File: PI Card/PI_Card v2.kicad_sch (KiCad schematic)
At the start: 20 parts, among them J1 Conn_02x20_Odd_Even, J2 Conn_02x20_Odd_Even, J3 Conn_01x03_Pin, J4 Conn_01x02, J5 Conn_02x40_Odd_Even, J6 Conn_01x03_Pin, SW1 SW_Push

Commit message: Repositioned Connections
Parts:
- D4: value PTVS5V0Z1USK -> SMAJ5.0A; footprint Diode_SMD:Nexperia_DSN1608-2_1.6x0.8mm -> Diode_SMD:D_SMA_Handsoldering
- H1, H2, H3, H4: footprint MountingHole:MountingHole_3.2mm_M3 -> MountingHole:MountingHole_2.2mm_M2
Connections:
- net GPIO10: now also J5.13 (Pin_13); no longer J5.19 (Pin_19)
- net GPIO11: now also J5.17 (Pin_17); no longer J5.23 (Pin_23)
- net GPIO12: now also J5.20 (Pin_20); no longer J5.32 (Pin_32)
- net GPIO13: now also J5.25 (Pin_25); no longer J5.33 (Pin_33)
- net GPIO14: now also J5.2 (Pin_2); no longer J5.8 (Pin_8)
- net GPIO15: now also J5.4 (Pin_4); no longer J5.10 (Pin_10)
- net GPIO16: now also J5.22 (Pin_22); no longer J5.36 (Pin_36)
- net GPIO17: now also J5.7 (Pin_7); no longer J5.11 (Pin_11)
- net GPIO18: now also J5.6 (Pin_6); no longer J5.12 (Pin_12)
- net GPIO19: now also J5.27 (Pin_27); no longer J5.35 (Pin_35)
- net GPIO2: now also J5.1 (Pin_1); no longer J5.3 (Pin_3)
- net GPIO20: now also J5.24 (Pin_24); no longer J5.38 (Pin_38)
- net GPIO21: now also J5.26 (Pin_26); no longer J5.40 (Pin_40)
- net GPIO22: now also J5.11 (Pin_11); no longer J5.15 (Pin_15)
- net GPIO23: now also J5.8 (Pin_8); no longer J5.16 (Pin_16)
- net GPIO24: now also J5.10 (Pin_10); no longer J5.18 (Pin_18)
- net GPIO25: now also J5.12 (Pin_12); no longer J5.22 (Pin_22)
- net GPIO26: now also J5.29 (Pin_29); no longer J5.37 (Pin_37)
- net GPIO27: now also J5.9 (Pin_9); no longer J5.13 (Pin_13)
- net GPIO3: now also J5.3 (Pin_3); no longer J5.5 (Pin_5)
- net GPIO4: now also J5.5 (Pin_5); no longer J5.7 (Pin_7)
- net GPIO5: now also J5.21 (Pin_21); no longer J5.29 (Pin_29)
- net GPIO6: now also J5.23 (Pin_23); no longer J5.31 (Pin_31)
- net GPIO7: now also J5.16 (Pin_16); no longer J5.26 (Pin_26)
- net GPIO8: now also J5.14 (Pin_14); no longer J5.24 (Pin_24)
- net GPIO9: now also J5.15 (Pin_15); no longer J5.21 (Pin_21)
- net ID_SC: now also J5.18 (Pin_18); no longer J5.28 (Pin_28)
- net ID_SD: now also J5.19 (Pin_19); no longer J5.27 (Pin_27)

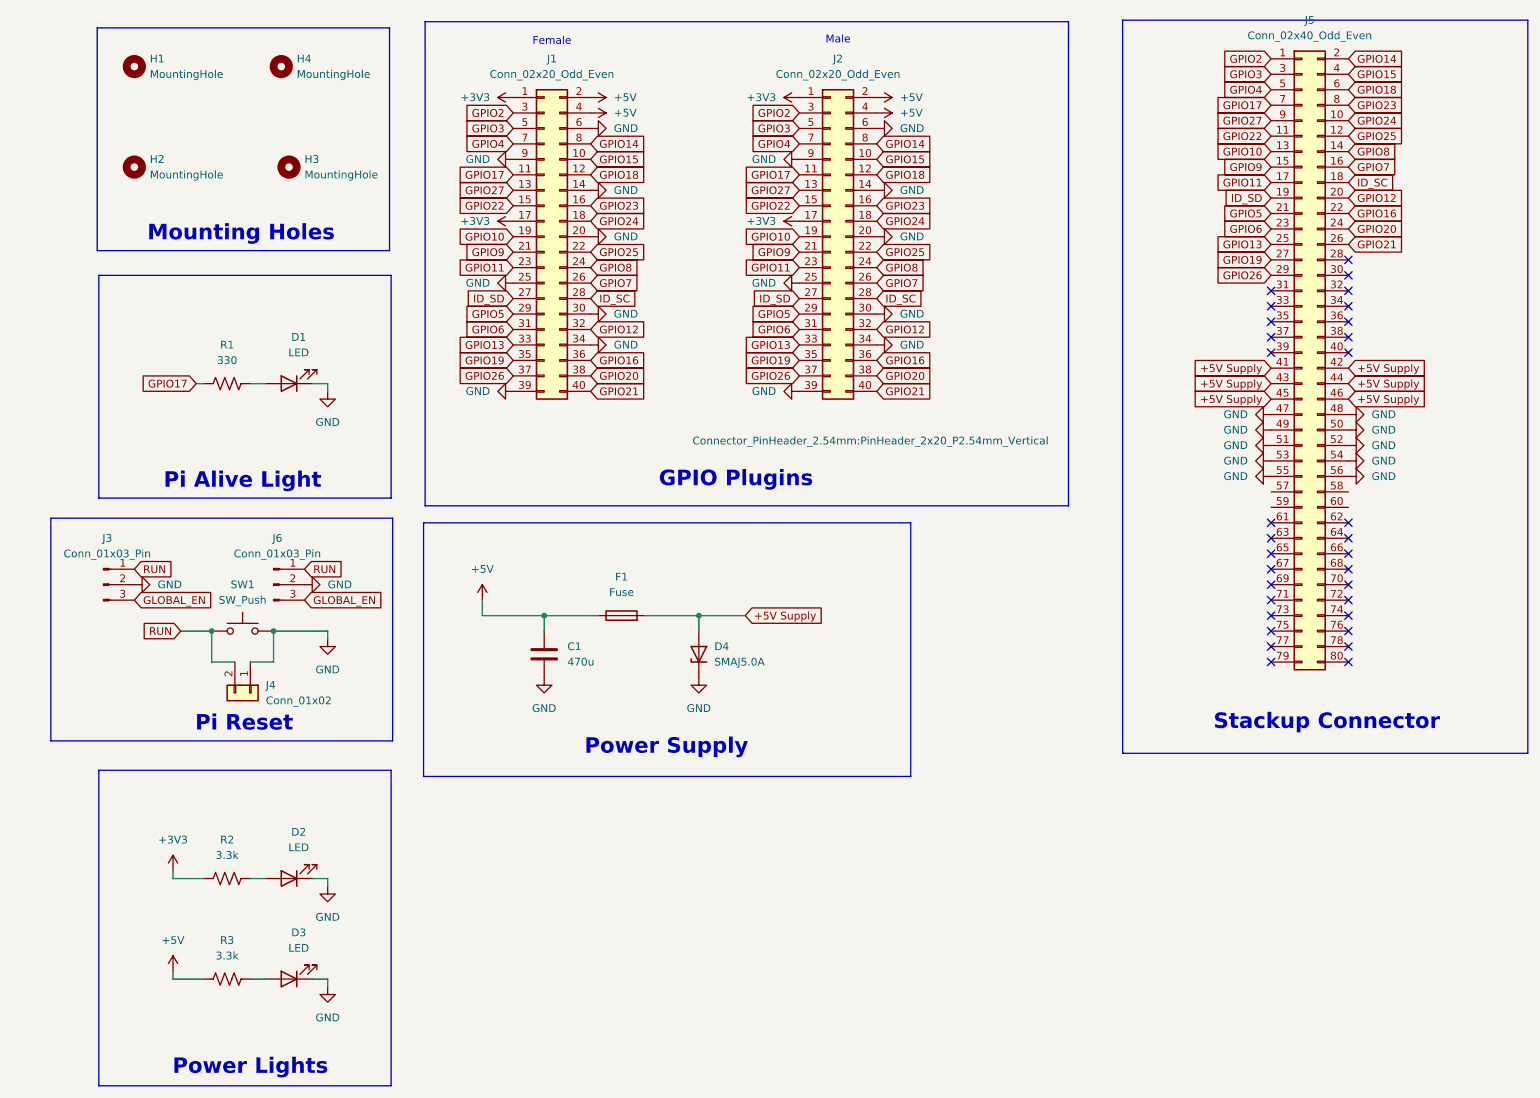
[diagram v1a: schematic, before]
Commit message: Added I2C & Reset Toggle
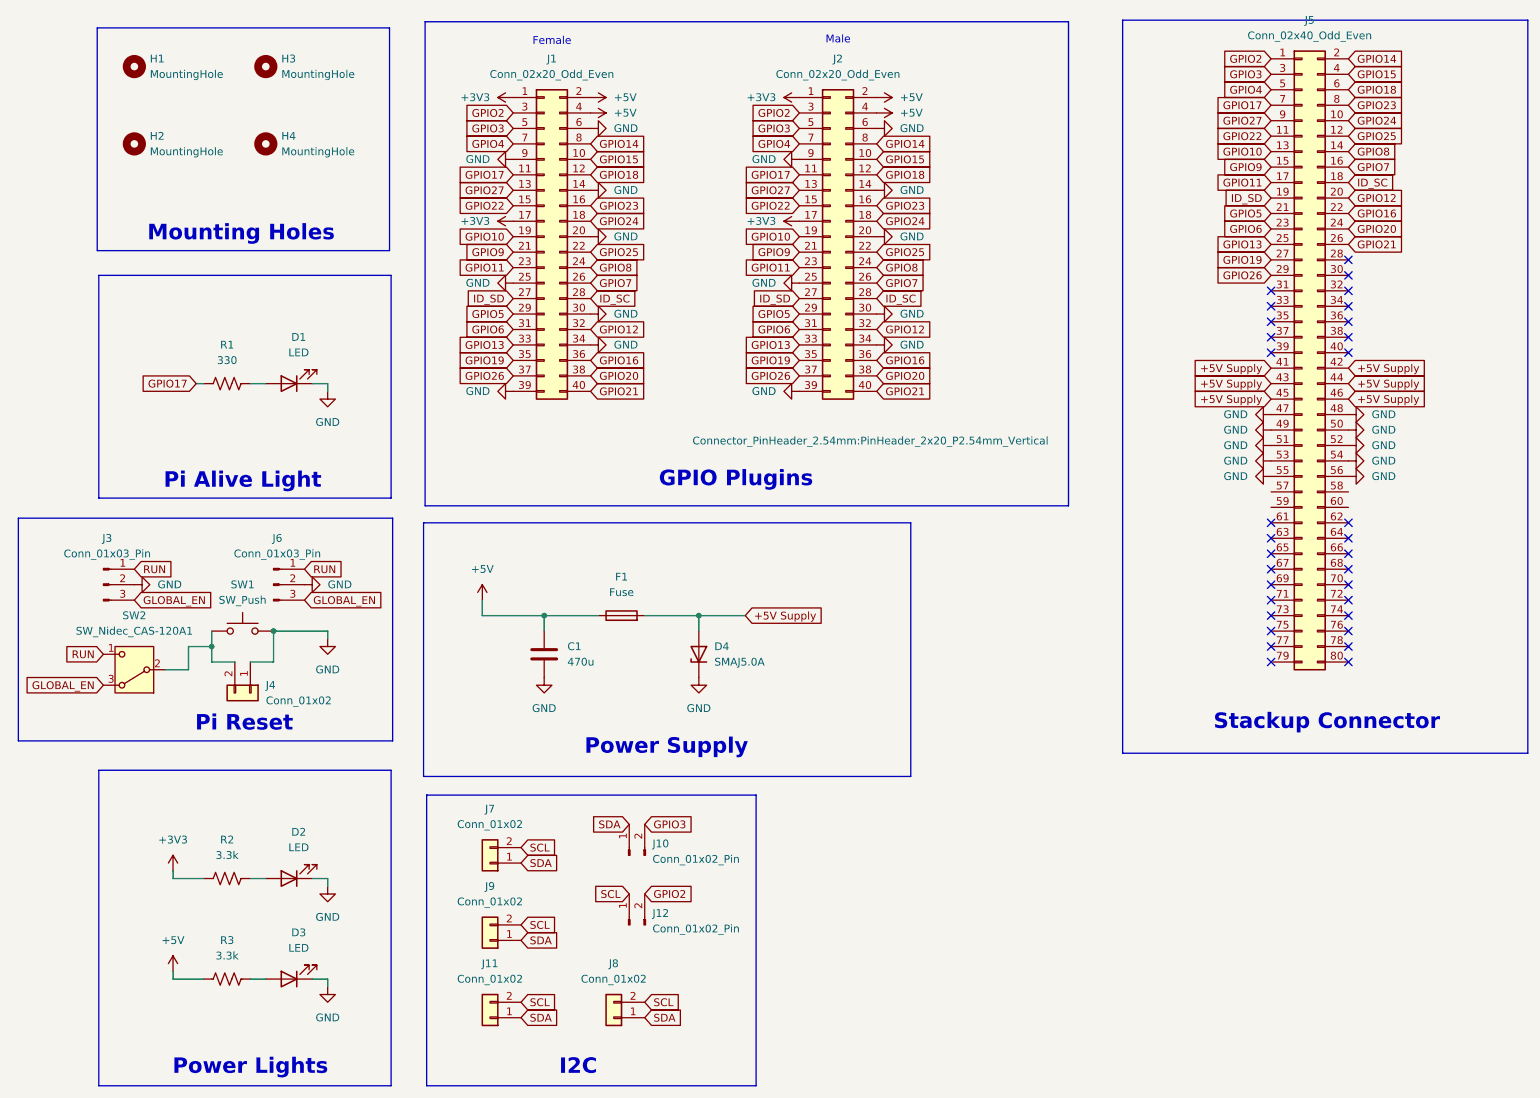
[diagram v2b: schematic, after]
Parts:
- added J10, J12: Conn_01x02_Pin, Connector_PinHeader_2.54mm:PinHeader_1x02_P2.54mm_Vertical, symbol Connector:Conn_01x02_Pin
- added J11, J7, J8, J9: Conn_01x02, Connector_JST:JST_PH_B2B-PH-K_1x02_P2.00mm_Vertical, symbol Connector_Generic:Conn_01x02
- added SW2: SW_Nidec_CAS-120A1, Button_Switch_SMD:Nidec_Copal_CAS-120A, symbol Switch:SW_Nidec_CAS-120A1
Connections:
- net GLOBAL_EN: now also SW2.3 (A)
- net GPIO2: now also J12.2 (Pin_2)
- net GPIO3: now also J10.2 (Pin_2)
- net RUN: now also SW2.1 (C); no longer J4.2 (Pin_2), SW1.1
- new net: J4.2 (Pin_2), SW1.1, SW2.2 (B)
- new net SCL: J11.2 (Pin_2), J12.1 (Pin_1), J7.2 (Pin_2), J8.2 (Pin_2), J9.2 (Pin_2)
- new net SDA: J10.1 (Pin_1), J11.1 (Pin_1), J7.1 (Pin_1), J8.1 (Pin_1), J9.1 (Pin_1)
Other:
- note added: "I2C"
- moved on the sheet: H2, H3, H4

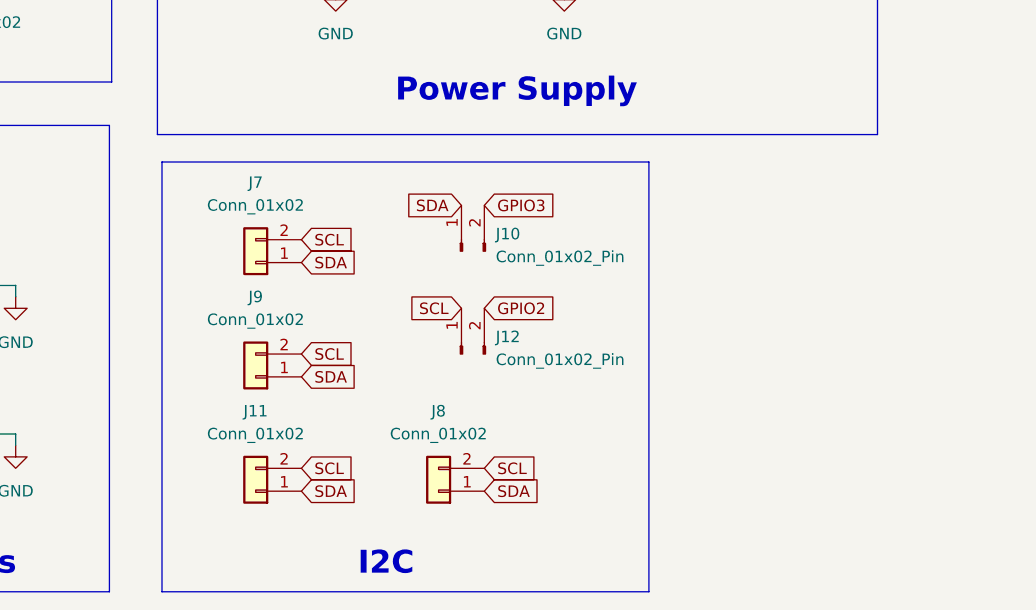
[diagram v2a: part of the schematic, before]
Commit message: Added I2C Pull Up Resistors
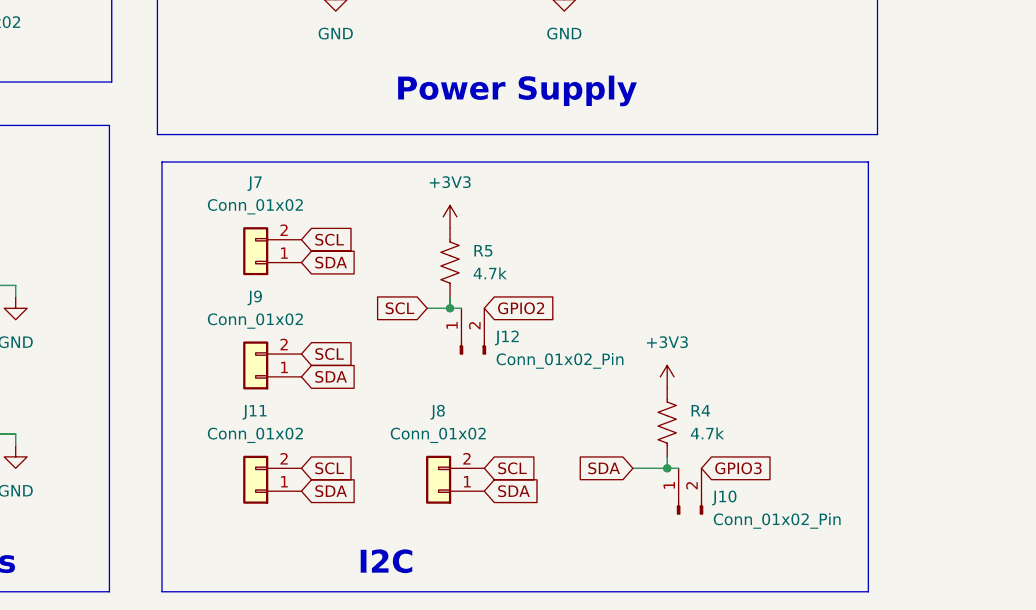
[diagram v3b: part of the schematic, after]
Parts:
- added R4, R5: 4.7k, Resistor_SMD:R_0805_2012Metric_Pad1.20x1.40mm_HandSolder, symbol Device:R_US
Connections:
- net +3V3: now also R4.2, R5.2
- net SCL: now also R5.1
- net SDA: now also R4.1
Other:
- moved on the sheet: J10
